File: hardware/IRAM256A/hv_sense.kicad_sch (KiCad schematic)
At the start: 16 parts

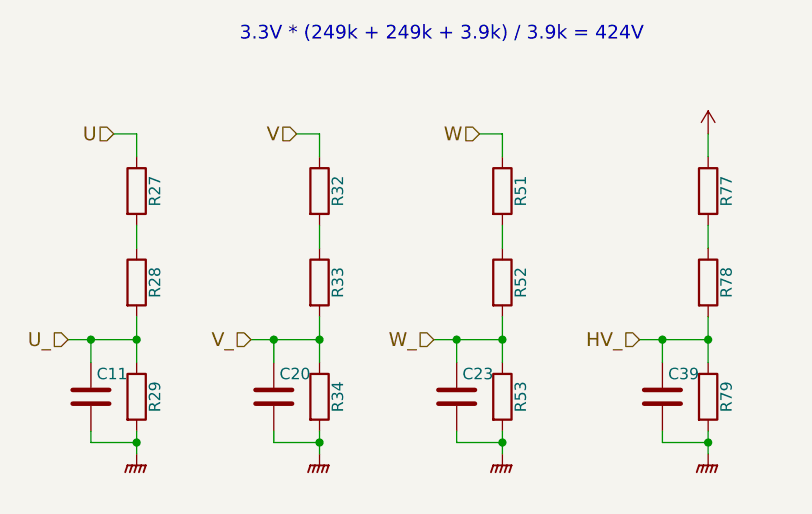
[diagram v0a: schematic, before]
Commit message: Structure change + kicad 3d models updated
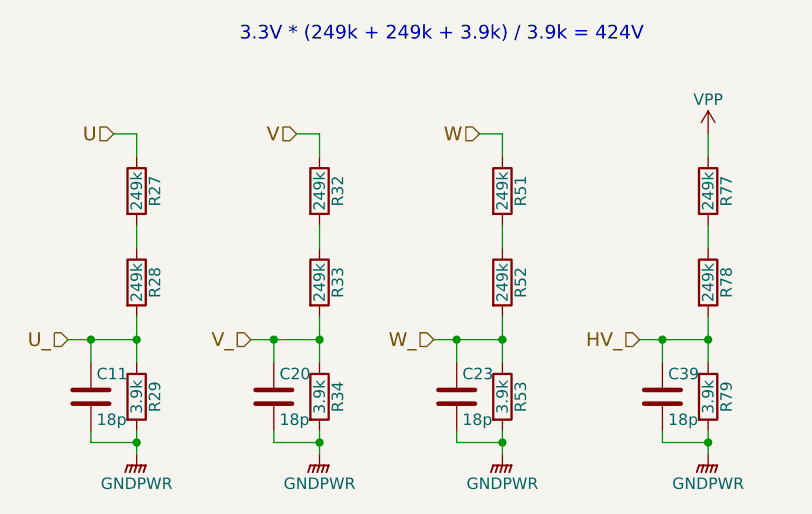
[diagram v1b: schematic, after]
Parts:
- C11, C20, C23, C39: value (none) -> 18p; footprint (none) -> stmbl:C_0603
- R27, R28, R32, R33, R51, R52, R77, R78: value (none) -> 249k; footprint (none) -> stmbl:R_1206
- R29, R34, R53, R79: value (none) -> 3.9k; footprint (none) -> stmbl:R_0603
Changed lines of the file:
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@@
     (in_bom yes) (on_board yes)
     (property "Reference" "R27" (id 0) (at 75.692 85.09 90))
-    (property "Value" "" (id 1) (at 73.66 85.09 90))
-    (property "Footprint" "" (id 2) (at 71.882 85.09 90)
+    (property "Value" "249k" (id 1) (at 73.66 85.09 90))
+    (property "Footprint" "stmbl:R_1206" (id 2) (at 71.882 85.09 90)
       (effects (font (size 0.762 0.762)) hide)
     )
@@
     (in_bom yes) (on_board yes)
     (property "Reference" "R28" (id 0) (at 75.692 95.25 90))
-    (property "Value" "" (id 1) (at 73.66 95.25 90))
-    (property "Footprint" "" (id 2) (at 71.882 95.25 90)
+    (property "Value" "249k" (id 1) (at 73.66 95.25 90))
+    (property "Footprint" "stmbl:R_1206" (id 2) (at 71.882 95.25 90)
       (effects (font (size 0.762 0.762)) hide)
     )
@@
     (in_bom yes) (on_board yes)
     (property "Reference" "R29" (id 0) (at 75.692 107.95 90))
-    (property "Value" "" (id 1) (at 73.66 107.95 90))
-    (property "Footprint" "" (id 2) (at 71.882 107.95 90)
+    (property "Value" "3.9k" (id 1) (at 73.66 107.95 90))
+    (property "Footprint" "stmbl:R_0603" (id 2) (at 71.882 107.95 90)
       (effects (font (size 0.762 0.762)) hide)
     )
@@
       (effects (font (size 1.27 1.27)) hide)
     )
-    (property "Value" "" (id 1) (at 73.66 117.602 0))
+    (property "Value" "GNDPWR" (id 1) (at 73.66 117.602 0))
     (property "Footprint" "" (id 2) (at 73.66 115.57 0)
       (effects (font (size 1.524 1.524)))
@@
     (in_bom yes) (on_board yes)
     (property "Reference" "R32" (id 0) (at 96.012 85.09 90))
-    (property "Value" "" (id 1) (at 93.98 85.09 90))
-    (property "Footprint" "" (id 2) (at 92.202 85.09 90)
+    (property "Value" "249k" (id 1) (at 93.98 85.09 90))
+    (property "Footprint" "stmbl:R_1206" (id 2) (at 92.202 85.09 90)
       (effects (font (size 0.762 0.762)) hide)
     )
@@
     (in_bom yes) (on_board yes)
     (property "Reference" "R33" (id 0) (at 96.012 95.25 90))
-    (property "Value" "" (id 1) (at 93.98 95.25 90))
-    (property "Footprint" "" (id 2) (at 92.202 95.25 90)
+    (property "Value" "249k" (id 1) (at 93.98 95.25 90))
+    (property "Footprint" "stmbl:R_1206" (id 2) (at 92.202 95.25 90)
       (effects (font (size 0.762 0.762)) hide)
     )
@@
     (in_bom yes) (on_board yes)
     (property "Reference" "R34" (id 0) (at 96.012 107.95 90))
-    (property "Value" "" (id 1) (at 93.98 107.95 90))
-    (property "Footprint" "" (id 2) (at 92.202 107.95 90)
+    (property "Value" "3.9k" (id 1) (at 93.98 107.95 90))
+    (property "Footprint" "stmbl:R_0603" (id 2) (at 92.202 107.95 90)
       (effects (font (size 0.762 0.762)) hide)
     )
@@
       (effects (font (size 1.27 1.27)) hide)
     )
-    (property "Value" "" (id 1) (at 93.98 117.602 0))
+    (property "Value" "GNDPWR" (id 1) (at 93.98 117.602 0))
     (property "Footprint" "" (id 2) (at 93.98 115.57 0)
       (effects (font (size 1.524 1.524)))
@@
     (in_bom yes) (on_board yes)
     (property "Reference" "R51" (id 0) (at 116.332 85.09 90))
-    (property "Value" "" (id 1) (at 114.3 85.09 90))
-    (property "Footprint" "" (id 2) (at 112.522 85.09 90)
+    (property "Value" "249k" (id 1) (at 114.3 85.09 90))
+    (property "Footprint" "stmbl:R_1206" (id 2) (at 112.522 85.09 90)
       (effects (font (size 0.762 0.762)) hide)
     )
@@
     (in_bom yes) (on_board yes)
     (property "Reference" "R52" (id 0) (at 116.332 95.25 90))
-    (property "Value" "" (id 1) (at 114.3 95.25 90))
-    (property "Footprint" "" (id 2) (at 112.522 95.25 90)
+    (property "Value" "249k" (id 1) (at 114.3 95.25 90))
+    (property "Footprint" "stmbl:R_1206" (id 2) (at 112.522 95.25 90)
       (effects (font (size 0.762 0.762)) hide)
     )
@@
     (in_bom yes) (on_board yes)
     (property "Reference" "R53" (id 0) (at 116.332 107.95 90))
-    (property "Value" "" (id 1) (at 114.3 107.95 90))
-    (property "Footprint" "" (id 2) (at 112.522 107.95 90)
+    (property "Value" "3.9k" (id 1) (at 114.3 107.95 90))
+    (property "Footprint" "stmbl:R_0603" (id 2) (at 112.522 107.95 90)
       (effects (font (size 0.762 0.762)) hide)
     )
@@
       (effects (font (size 1.27 1.27)) hide)
     )
-    (property "Value" "" (id 1) (at 114.3 117.602 0))
+    (property "Value" "GNDPWR" (id 1) (at 114.3 117.602 0))
     (property "Footprint" "" (id 2) (at 114.3 115.57 0)
       (effects (font (size 1.524 1.524)))
@@
     (in_bom yes) (on_board yes)
     (property "Reference" "R77" (id 0) (at 139.192 85.09 90))
-    (property "Value" "" (id 1) (at 137.16 85.09 90))
-    (property "Footprint" "" (id 2) (at 135.382 85.09 90)
+    (property "Value" "249k" (id 1) (at 137.16 85.09 90))
+    (property "Footprint" "stmbl:R_1206" (id 2) (at 135.382 85.09 90)
       (effects (font (size 0.762 0.762)) hide)
     )
@@
     (in_bom yes) (on_board yes)
     (property "Reference" "R78" (id 0) (at 139.192 95.25 90))
-    (property "Value" "" (id 1) (at 137.16 95.25 90))
-    (property "Footprint" "" (id 2) (at 135.382 95.25 90)
+    (property "Value" "249k" (id 1) (at 137.16 95.25 90))
+    (property "Footprint" "stmbl:R_1206" (id 2) (at 135.382 95.25 90)
       (effects (font (size 0.762 0.762)) hide)
     )
@@
     (in_bom yes) (on_board yes)
     (property "Reference" "R79" (id 0) (at 139.192 107.95 90))
-    (property "Value" "" (id 1) (at 137.16 107.95 90))
-    (property "Footprint" "" (id 2) (at 135.382 107.95 90)
+    (property "Value" "3.9k" (id 1) (at 137.16 107.95 90))
+    (property "Footprint" "stmbl:R_0603" (id 2) (at 135.382 107.95 90)
       (effects (font (size 0.762 0.762)) hide)
     )
@@
       (effects (font (size 1.27 1.27)) hide)
     )
-    (property "Value" "" (id 1) (at 137.16 117.602 0))
+    (property "Value" "GNDPWR" (id 1) (at 137.16 117.602 0))
     (property "Footprint" "" (id 2) (at 137.16 115.57 0)
       (effects (font (size 1.524 1.524)))
@@
       (effects (font (size 1.27 1.27)) (justify left))
     )
-    (property "Value" "" (id 1) (at 69.215 110.49 0)
-      (effects (font (size 1.27 1.27)) (justify left))
-    )
-    (property "Footprint" "" (id 2) (at 69.5452 111.76 0)
+    (property "Value" "18p" (id 1) (at 69.215 110.49 0)
+      (effects (font (size 1.27 1.27)) (justify left))
+    )
+    (property "Footprint" "stmbl:C_0603" (id 2) (at 69.5452 111.76 0)
       (effects (font (size 0.762 0.762)) hide)
     )
@@
       (effects (font (size 1.27 1.27)) (justify left))
     )
-    (property "Value" "" (id 1) (at 89.535 110.49 0)
-      (effects (font (size 1.27 1.27)) (justify left))
-    )
-    (property "Footprint" "" (id 2) (at 89.8652 111.76 0)
+    (property "Value" "18p" (id 1) (at 89.535 110.49 0)
+      (effects (font (size 1.27 1.27)) (justify left))
+    )
+    (property "Footprint" "stmbl:C_0603" (id 2) (at 89.8652 111.76 0)
       (effects (font (size 0.762 0.762)) hide)
     )
@@
       (effects (font (size 1.27 1.27)) (justify left))
     )
-    (property "Value" "" (id 1) (at 109.855 110.49 0)
-      (effects (font (size 1.27 1.27)) (justify left))
-    )
-    (property "Footprint" "" (id 2) (at 110.1852 111.76 0)
+    (property "Value" "18p" (id 1) (at 109.855 110.49 0)
+      (effects (font (size 1.27 1.27)) (justify left))
+    )
+    (property "Footprint" "stmbl:C_0603" (id 2) (at 110.1852 111.76 0)
       (effects (font (size 0.762 0.762)) hide)
     )
@@
       (effects (font (size 1.27 1.27)) (justify left))
     )
-    (property "Value" "" (id 1) (at 132.715 110.49 0)
-      (effects (font (size 1.27 1.27)) (justify left))
-    )
-    (property "Footprint" "" (id 2) (at 133.0452 111.76 0)
+    (property "Value" "18p" (id 1) (at 132.715 110.49 0)
+      (effects (font (size 1.27 1.27)) (justify left))
+    )
+    (property "Footprint" "stmbl:C_0603" (id 2) (at 133.0452 111.76 0)
       (effects (font (size 0.762 0.762)) hide)
     )
@@
       (effects (font (size 1.27 1.27)) hide)
     )
-    (property "Value" "" (id 1) (at 137.16 74.93 0))
+    (property "Value" "VPP" (id 1) (at 137.16 74.93 0))
     (property "Footprint" "" (id 2) (at 137.16 78.74 0))
     (property "Datasheet" "" (id 3) (at 137.16 78.74 0))
